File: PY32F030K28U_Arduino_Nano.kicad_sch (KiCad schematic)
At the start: 28 parts, among them J1 USB_C_Receptacle_USB2.0, J41 DAPLINK, Q1 AO3401A, Q2 2N7002DW, U1 ME6211CxxU4AG, U2 PY32F030K2xU, U3 CH343P, U4 Arduino Nano, Y1 24M

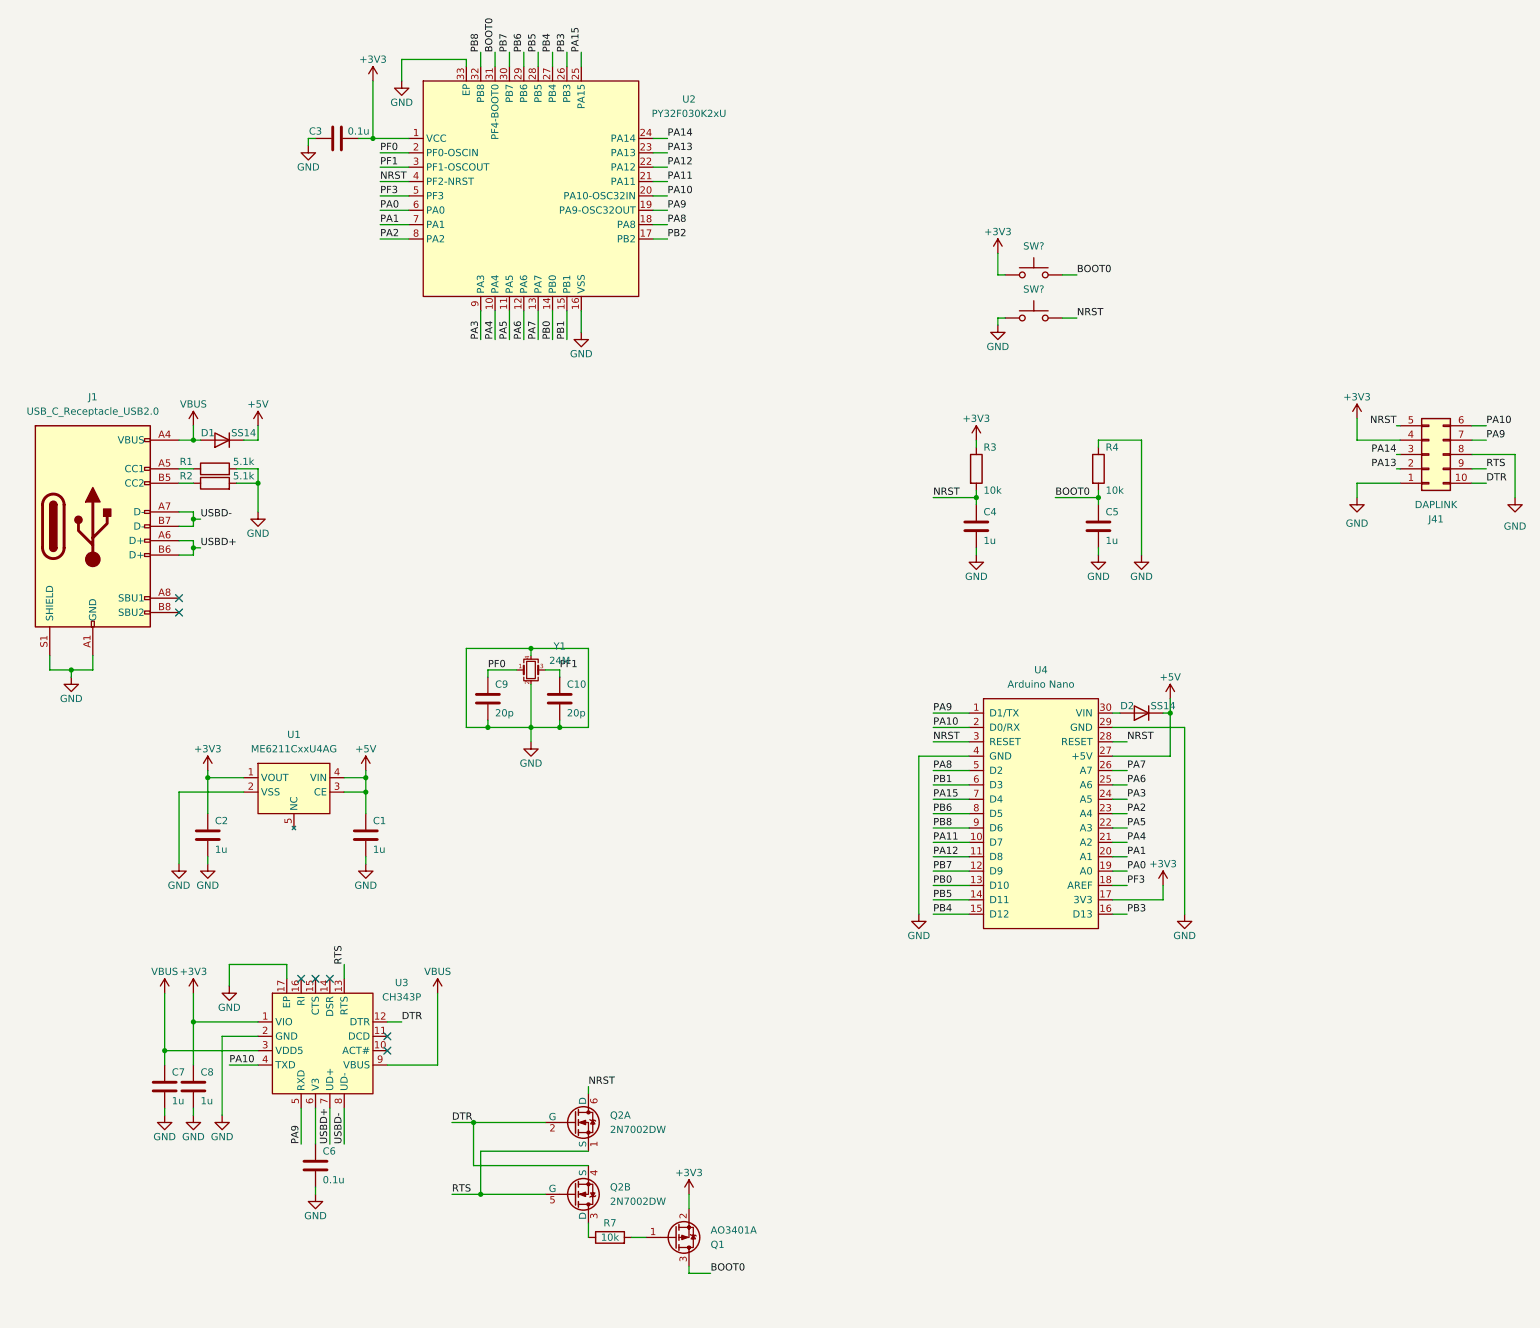
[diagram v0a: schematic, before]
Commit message: corrected DRC errors in PCB design
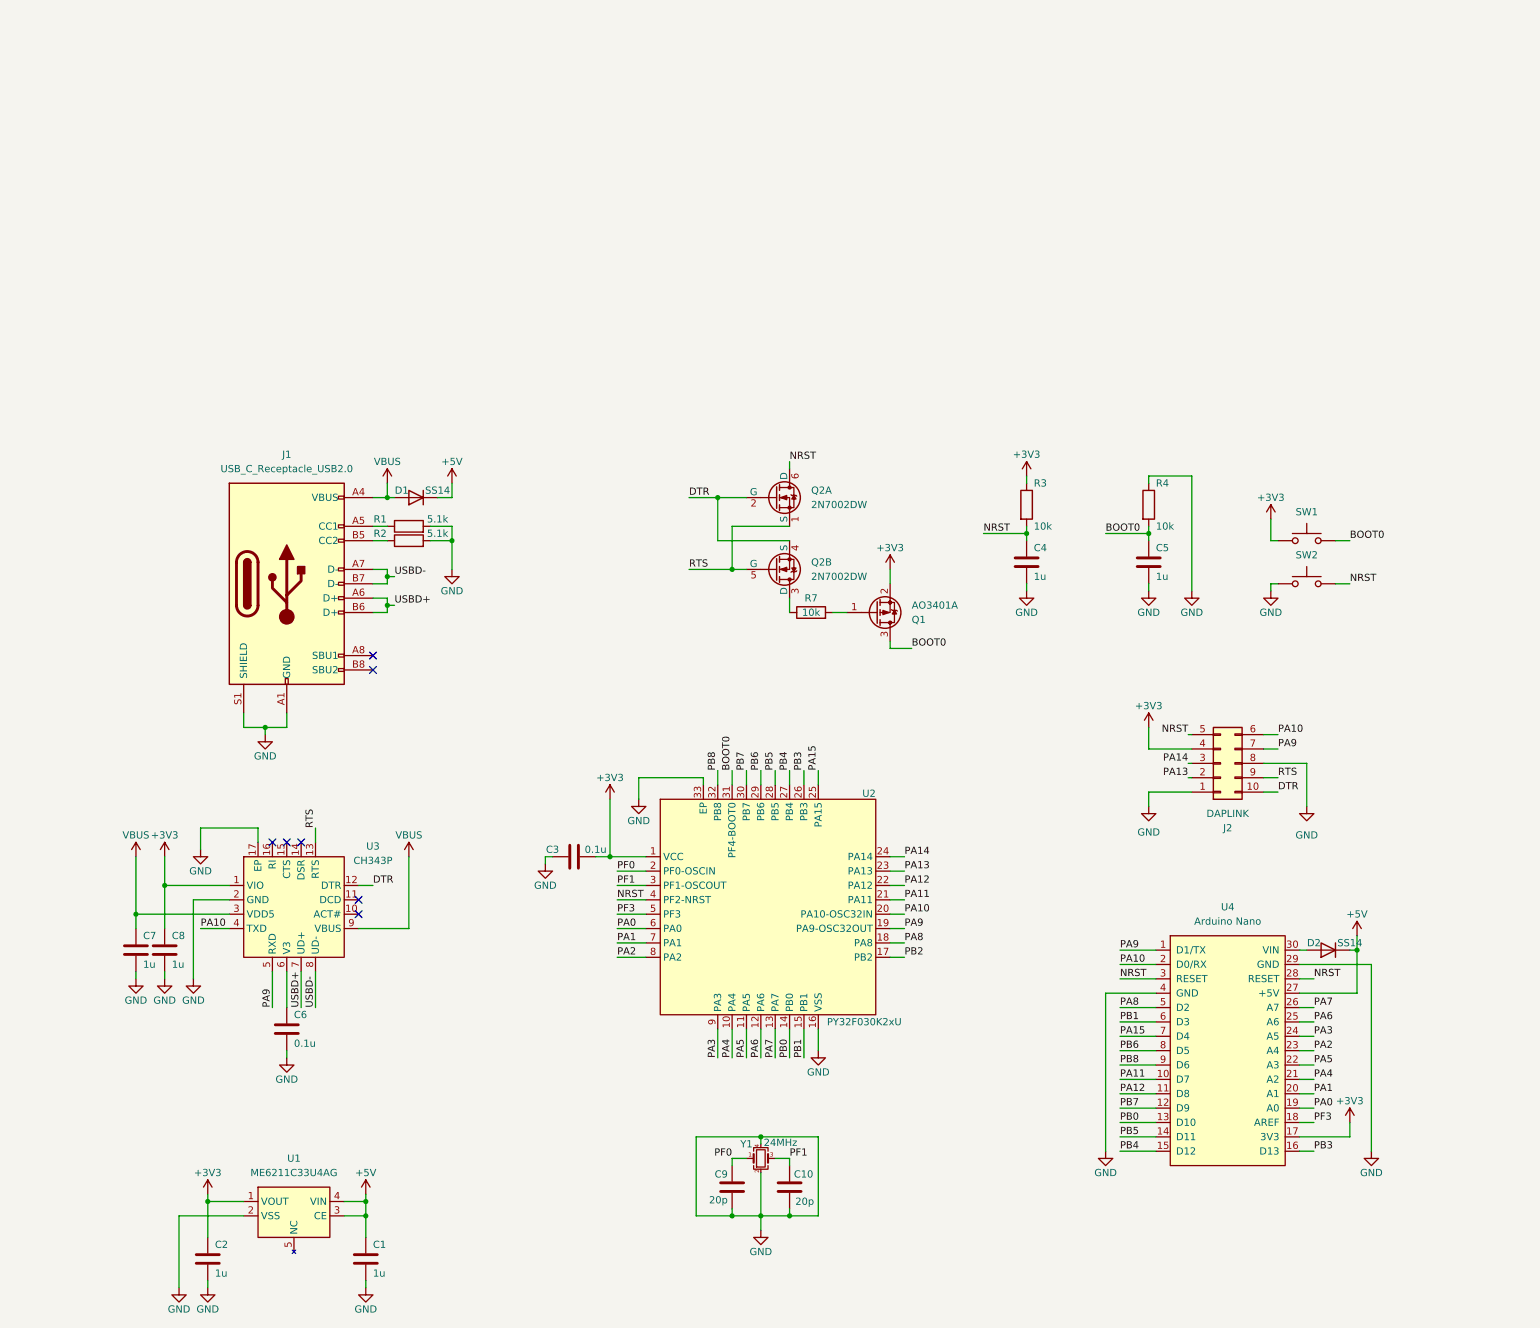
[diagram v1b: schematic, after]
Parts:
- U1: value ME6211CxxU4AG -> ME6211C33U4AG
- Y1: value 24M -> 24MHz
- gave numbers to parts that had none: 2
- renumbered J41 to J2
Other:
- moved on the sheet: C1, C10, C2, C3, C4, C5, C6, C7, C8, C9, D1, D2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
